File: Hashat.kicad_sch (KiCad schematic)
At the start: 1 part

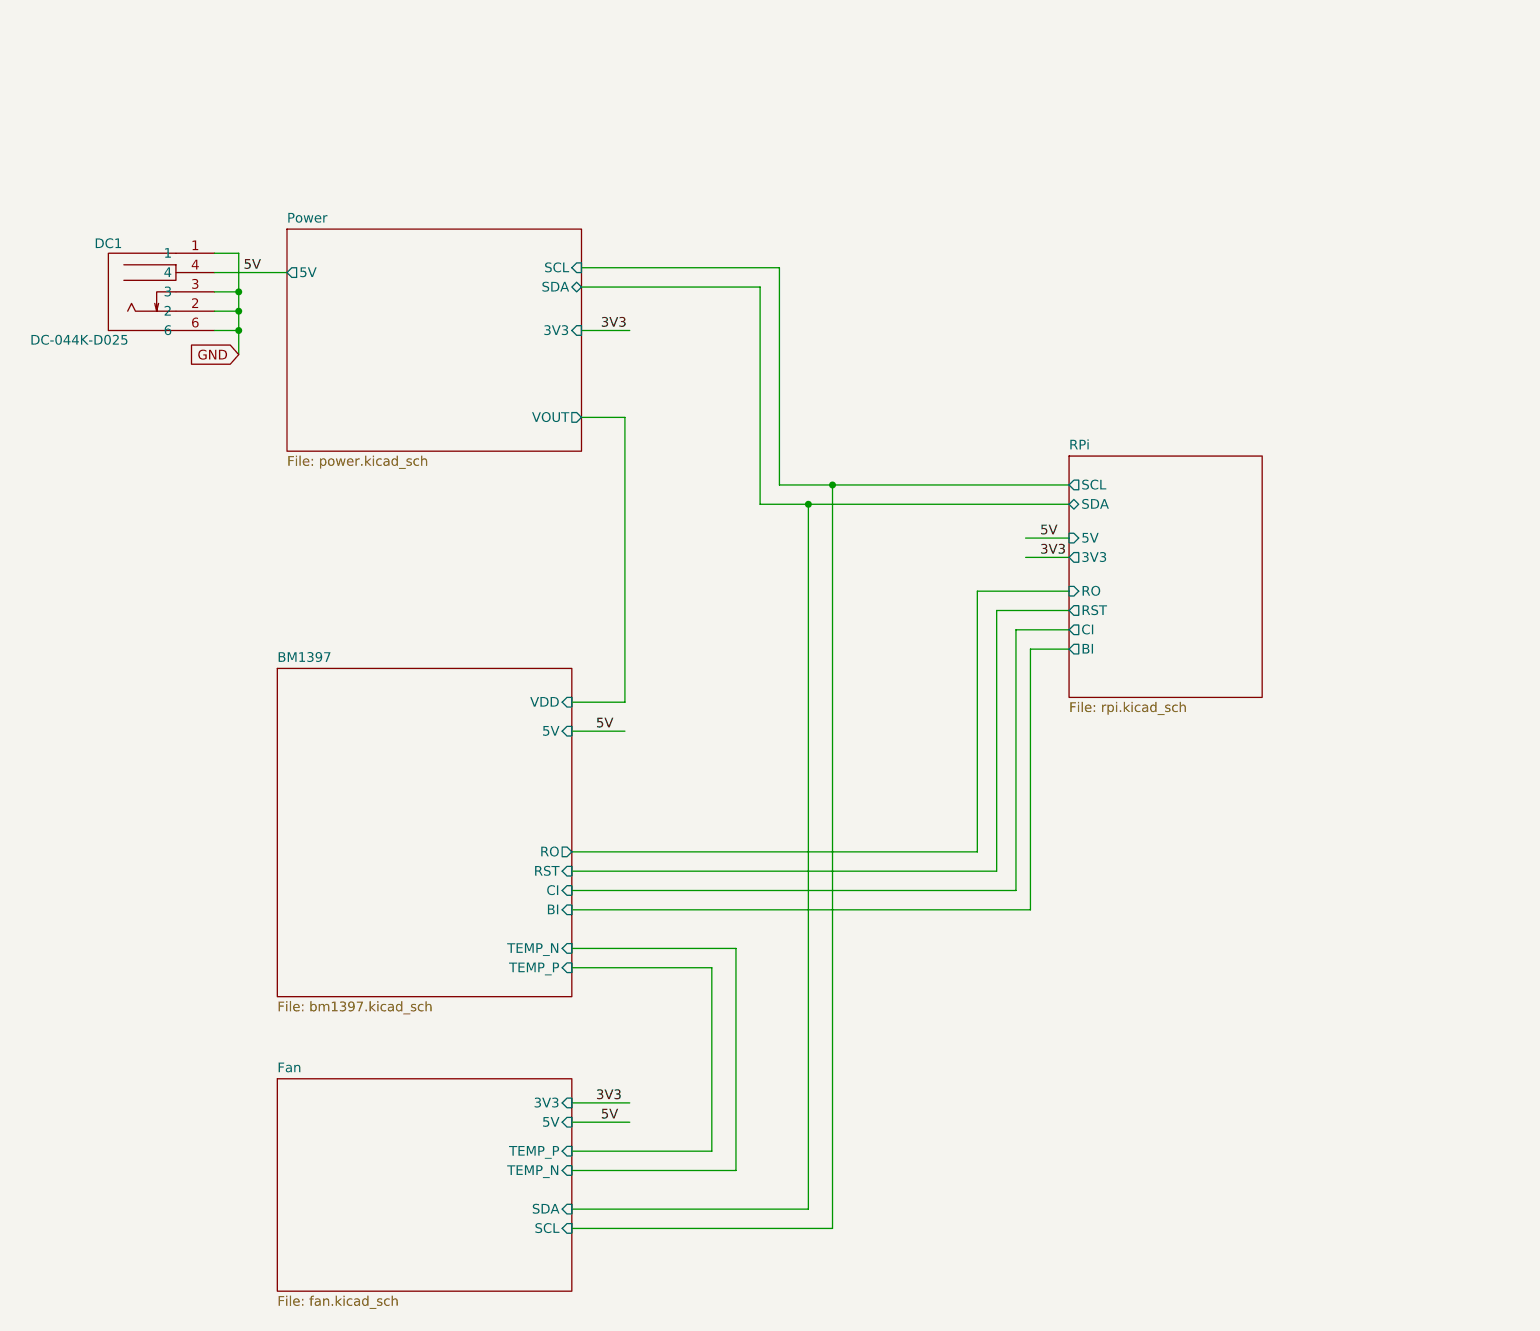
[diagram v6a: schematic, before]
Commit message: added 4 discrete level shifters with LCSC stock
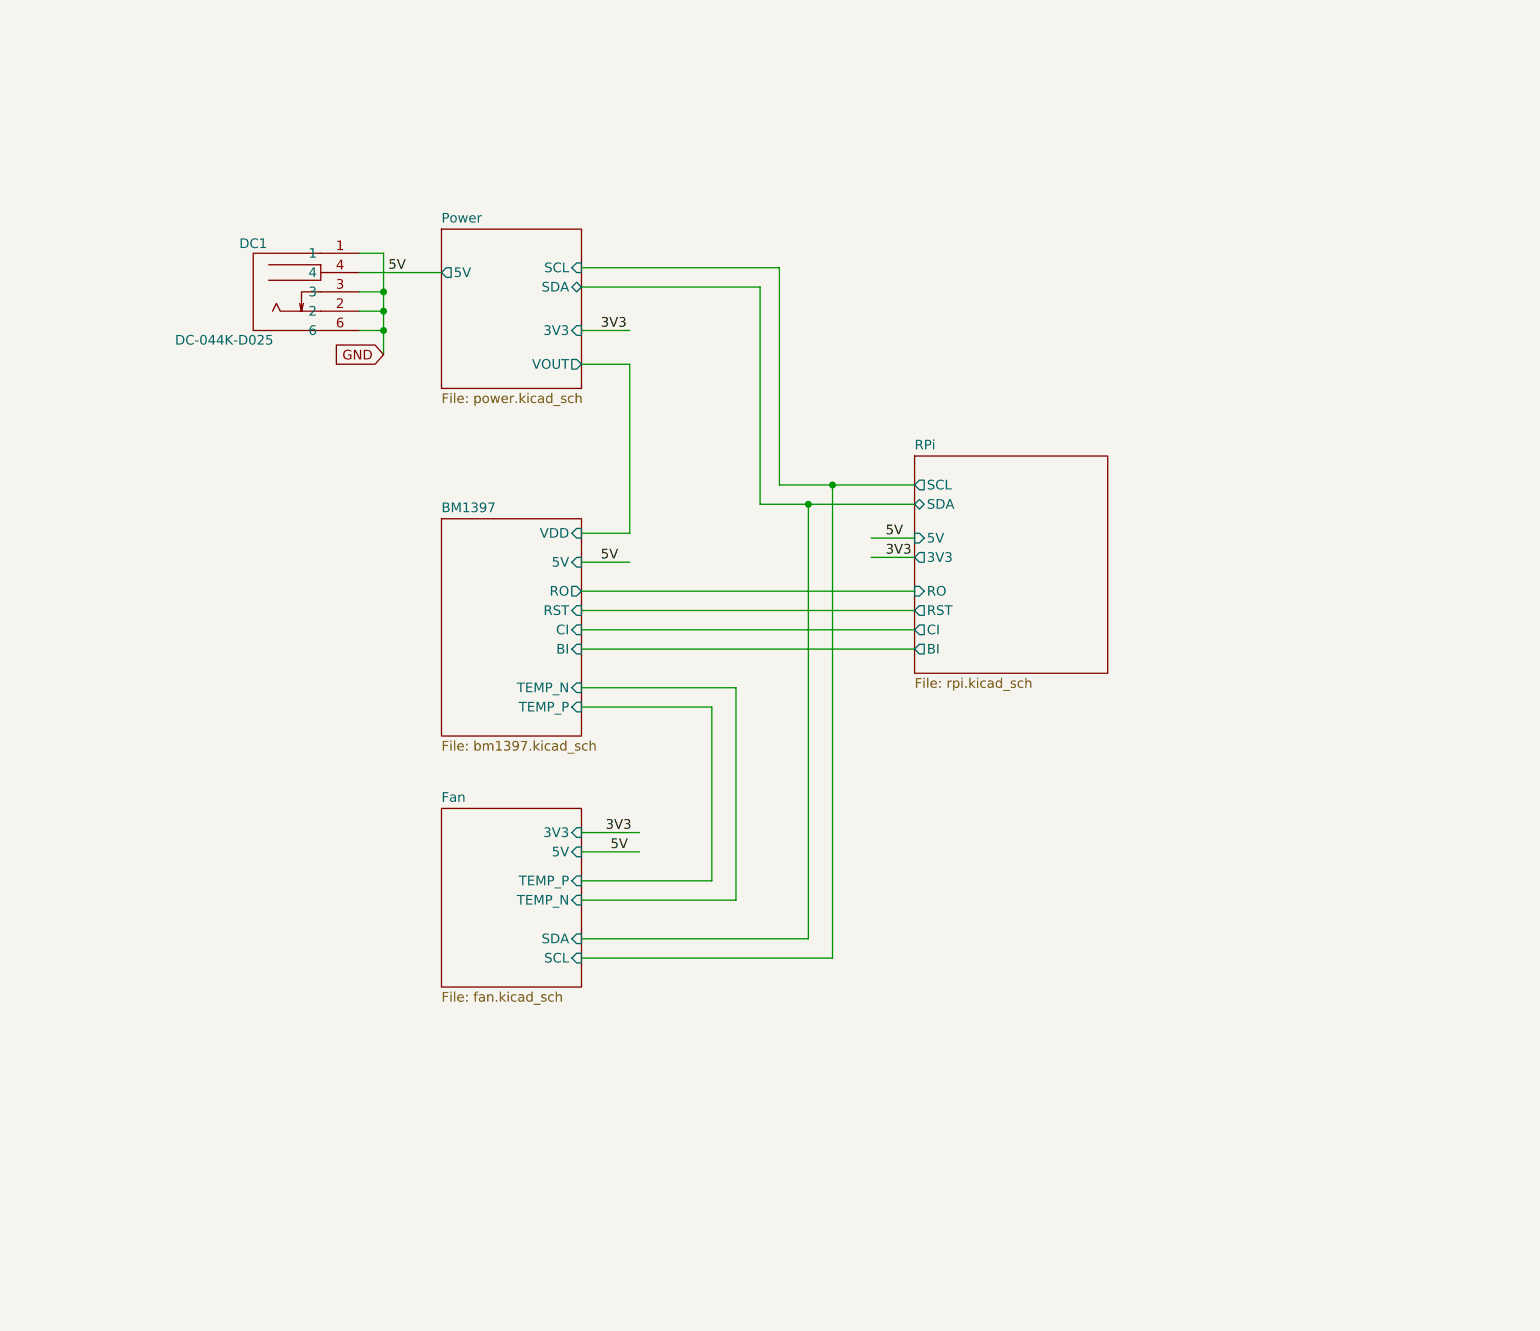
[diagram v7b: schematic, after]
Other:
- moved on the sheet: DC1

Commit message: matched up layout ref with schematic
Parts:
- added H1, H2, H3, H4: AlignmentHole, MountingHole:MountingHole_2.2mm_M2, symbol Mechanical:MountingHole
- added H5, H6: MountingHole, MountingHole:MountingHole_3.5mm, symbol Mechanical:MountingHole
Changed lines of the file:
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@@
+    )
+  )
+  (symbol (lib_id "Mechanical:MountingHole") (at 74.93 173.355 0) (unit 1)
+    (in_bom yes) (on_board yes) (dnp no) (fields_autoplaced)
+    (property "Reference" "H3" (at 77.47 172.0849 0)
+      (effects (font (size 1.27 1.27)) (justify left))
+    )
+    (property "Value" "AlignmentHole" (at 77.47 174.6249 0)
+      (effects (font (size 1.27 1.27)) (justify left))
+    )
+    (property "Footprint" "MountingHole:MountingHole_2.2mm_M2" (at 74.93 173.355 0)
+      (effects (font (size 1.27 1.27)) hide)
+    )
+    (property "Datasheet" "~" (at 74.93 173.355 0)
+      (effects (font (size 1.27 1.27)) hide)
+    )
+    (property "PARTNO" "https://www.amazon.com/dp/B07MDFS1YS" (at 74.93 173.355 0)
+      (effects (font (size 1.27 1.27)) hide)
+    )
+    (property "DNP" "T" (at 74.93 173.355 0)
+      (effects (font (size 1.27 1.27)) hide)
+    )
+    (instances
+      (project "Hashat"
+        (path "/00740941-7ad8-466a-a267-188591e2b5c4"
+          (reference "H3") (unit 1)
+        )
+      )
+      (project "bitaxeMax"
+        (path "/e63e39d7-6ac0-4ffd-8aa3-1841a4541b55"
+          (reference "H3") (unit 1)
+        )
+      )
+    )
+  )
+  (symbol (lib_id "Mechanical:MountingHole") (at 100.965 172.72 0) (unit 1)
+    (in_bom yes) (on_board yes) (dnp no) (fields_autoplaced)
+    (property "Reference" "H5" (at 103.505 171.4499 0)
+      (effects (font (size 1.27 1.27)) (justify left))
+    )
+    (property "Value" "MountingHole" (at 103.505 173.9899 0)
+      (effects (font (size 1.27 1.27)) (justify left))
+    )
+    (property "Footprint" "MountingHole:MountingHole_3.5mm" (at 100.965 172.72 0)
+      (effects (font (size 1.27 1.27)) hide)
+    )
+    (property "Datasheet" "~" (at 100.965 172.72 0)
+      (effects (font (size 1.27 1.27)) hide)
+    )
+    (property "DNP" "T" (at 100.965 172.72 0)
+      (effects (font (size 1.27 1.27)) hide)
+    )
+    (instances
+      (project "Hashat"
+        (path "/00740941-7ad8-466a-a267-188591e2b5c4"
+          (reference "H5") (unit 1)
+        )
+      )
+      (project "bitaxeMax"
+        (path "/e63e39d7-6ac0-4ffd-8aa3-1841a4541b55"
+          (reference "H5") (unit 1)
+        )
+      )
     )
   )
@@
         )
       )
+    )
+  )
+  (symbol (lib_id "Mechanical:MountingHole") (at 100.965 180.34 0) (unit 1)
+    (in_bom yes) (on_board yes) (dnp no) (fields_autoplaced)
+    (property "Reference" "H6" (at 103.505 179.0699 0)
+      (effects (font (size 1.27 1.27)) (justify left))
+    )
+    (property "Value" "MountingHole" (at 103.505 181.6099 0)
+      (effects (font (size 1.27 1.27)) (justify left))
+    )
+    (property "Footprint" "MountingHole:MountingHole_3.5mm" (at 100.965 180.34 0)
+      (effects (font (size 1.27 1.27)) hide)
+    )
+    (property "Datasheet" "~" (at 100.965 180.34 0)
+      (effects (font (size 1.27 1.27)) hide)
+    )
+    (property "DNP" "T" (at 100.965 180.34 0)
+      (effects (font (size 1.27 1.27)) hide)
+    )
+    (instances
+      (project "Hashat"
+        (path "/00740941-7ad8-466a-a267-188591e2b5c4"
+          (reference "H6") (unit 1)
+        )
+      )
+      (project "bitaxeMax"
+        (path "/e63e39d7-6ac0-4ffd-8aa3-1841a4541b55"
+          (reference "H6") (unit 1)
+        )
+      )
+    )
+  )
+  (symbol (lib_id "Mechanical:MountingHole") (at 74.93 160.655 0) (unit 1)
+    (in_bom yes) (on_board yes) (dnp no) (fields_autoplaced)
+    (property "Reference" "H1" (at 77.47 159.3849 0)
+      (effects (font (size 1.27 1.27)) (justify left))
+    )
+    (property "Value" "AlignmentHole" (at 77.47 161.9249 0)
+      (effects (font (size 1.27 1.27)) (justify left))
+    )
+    (property "Footprint" "MountingHole:MountingHole_2.2mm_M2" (at 74.93 160.655 0)
+      (effects (font (size 1.27 1.27)) hide)
+    )
+    (property "Datasheet" "~" (at 74.93 160.655 0)
+      (effects (font (size 1.27 1.27)) hide)
+    )
+    (property "PARTNO" "https://www.amazon.com/dp/B07MDFS1YS" (at 74.93 160.655 0)
+      (effects (font (size 1.27 1.27)) hide)
+    )
+    (property "DNP" "T" (at 74.93 160.655 0)
+      (effects (font (size 1.27 1.27)) hide)
+    )
+    (instances
+      (project "Hashat"
+        (path "/00740941-7ad8-466a-a267-188591e2b5c4"
+          (reference "H1") (unit 1)
+        )
+      )
+      (project "bitaxeMax"
+        (path "/e63e39d7-6ac0-4ffd-8aa3-1841a4541b55"
+          (reference "H1") (unit 1)
+        )
+      )
+    )
+  )
+  (symbol (lib_id "Mechanical:MountingHole") (at 74.93 180.34 0) (unit 1)
+    (in_bom yes) (on_board yes) (dnp no) (fields_autoplaced)
+    (property "Reference" "H4" (at 77.47 179.0699 0)
+      (effects (font (size 1.27 1.27)) (justify left))
+    )
+    (property "Value" "AlignmentHole" (at 77.47 181.6099 0)
+      (effects (font (size 1.27 1.27)) (justify left))
+    )
+    (property "Footprint" "MountingHole:MountingHole_2.2mm_M2" (at 74.93 180.34 0)
+      (effects (font (size 1.27 1.27)) hide)
+    )
+    (property "Datasheet" "~" (at 74.93 180.34 0)
+      (effects (font (size 1.27 1.27)) hide)
+    )
+    (property "PARTNO" "https://www.amazon.com/dp/B07MDFS1YS" (at 74.93 180.34 0)
+      (effects (font (size 1.27 1.27)) hide)
+    )
+    (property "DNP" "T" (at 74.93 180.34 0)
+      (effects (font (size 1.27 1.27)) hide)
+    )
+    (instances
+      (project "Hashat"
+        (path "/00740941-7ad8-466a-a267-188591e2b5c4"
+          (reference "H4") (unit 1)
+        )
+      )
+      (project "bitaxeMax"
+        (path "/e63e39d7-6ac0-4ffd-8aa3-1841a4541b55"
+          (reference "H4") (unit 1)
+        )
+      )
+    )
+  )
+  (symbol (lib_id "Mechanical:MountingHole") (at 74.93 167.005 0) (unit 1)
+    (in_bom yes) (on_board yes) (dnp no) (fields_autoplaced)
+    (property "Reference" "H2" (at 77.47 165.7349 0)
+      (effects (font (size 1.27 1.27)) (justify left))
+    )
+    (property "Value" "AlignmentHole" (at 77.47 168.2749 0)
+      (effects (font (size 1.27 1.27)) (justify left))
+    )
+    (property "Footprint" "MountingHole:MountingHole_2.2mm_M2" (at 74.93 167.005 0)
+      (effects (font (size 1.27 1.27)) hide)
+    )
+    (property "Datasheet" "~" (at 74.93 167.005 0)
+      (effects (font (size 1.27 1.27)) hide)
+    )
+    (property "PARTNO" "https://www.amazon.com/dp/B07MDFS1YS" (at 74.93 167.005 0)
+      (effects (font (size 1.27 1.27)) hide)
+    )
+    (property "DNP" "T" (at 74.93 167.005 0)
+      (effects (font (size 1.27 1.27)) hide)
+    )
+    (instances
+      (project "Hashat"
+        (path "/00740941-7ad8-466a-a267-188591e2b5c4"
+          (reference "H2") (unit 1)
+        )
+      )
+      (project "bitaxeMax"
+        (path "/e63e39d7-6ac0-4ffd-8aa3-1841a4541b55"
+          (reference "H2") (unit 1)
+        )
+      )
